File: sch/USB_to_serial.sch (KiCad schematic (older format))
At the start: 4 parts, among them J2 USB_B_Micro, U2 CP2102, U4 TPD2S017

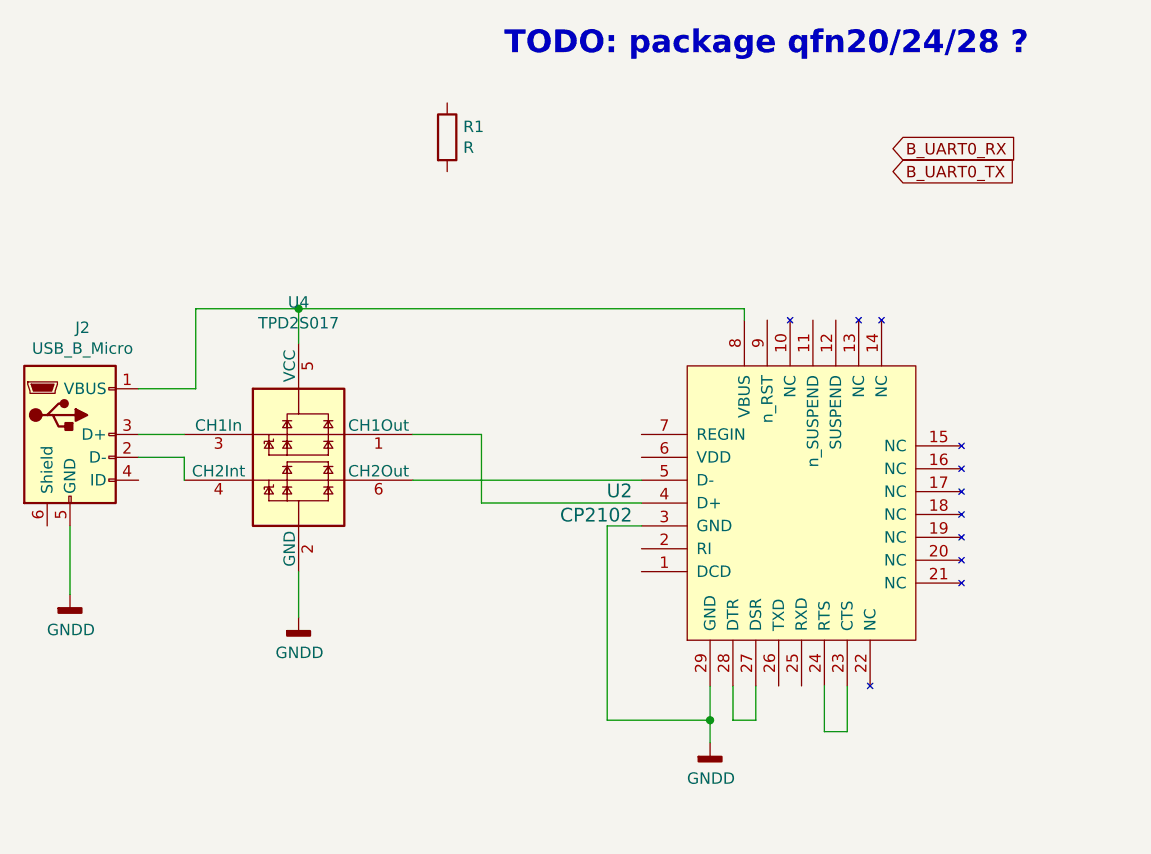
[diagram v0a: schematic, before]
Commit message: add u-boot sources
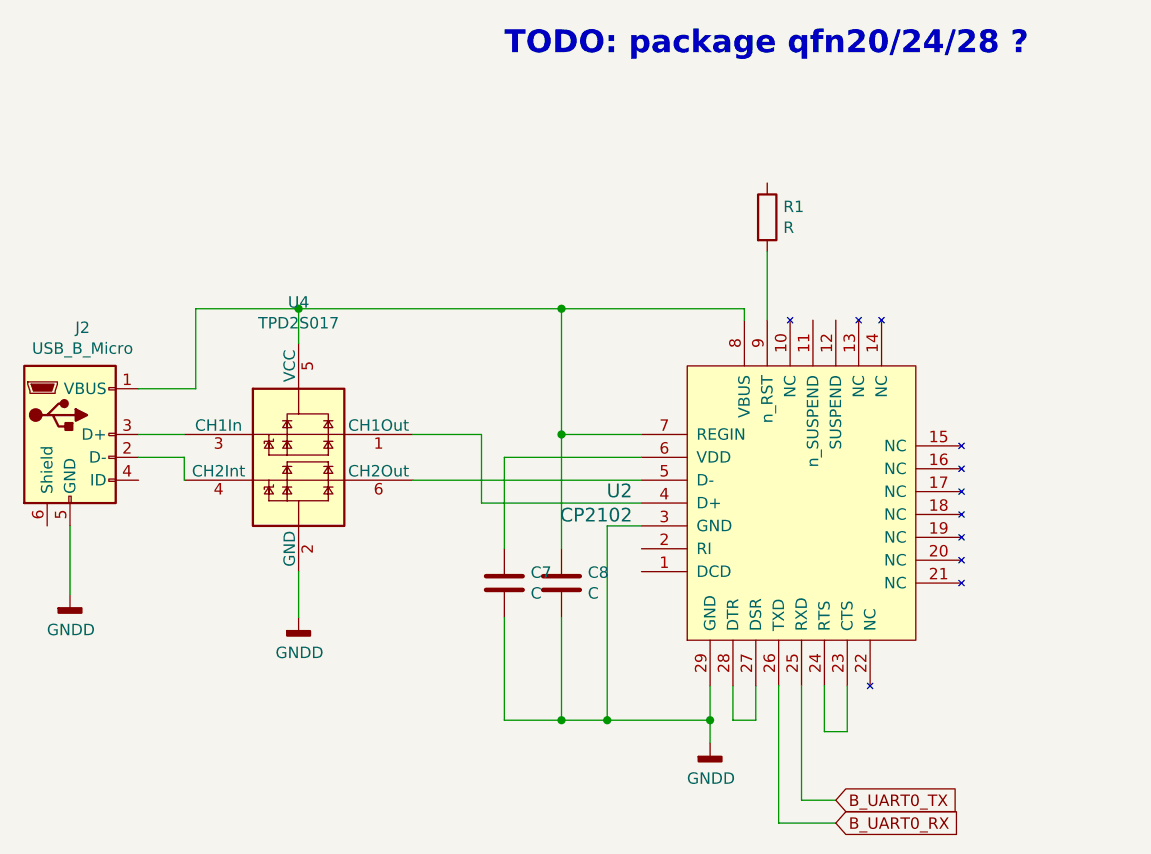
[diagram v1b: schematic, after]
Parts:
- added C7, C8: C, Capacitor_SMD:C_0805_2012Metric, symbol Device:C
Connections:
- net B_UART0_RX: now also U2.26 (TXD)
- net B_UART0_TX: now also U2.25 (RXD)
- net GNDD: now also C7.2, C8.1
- net at J2.1 (VBUS), U2.8 (VBUS), U4.5 (VCC): now also U2.7 (REGIN), C8.2
- net at R1.2: now also U2.9 (n_RST)
- net at U2.6 (VDD): now also C7.1
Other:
- moved on the sheet: R1
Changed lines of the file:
@@
 EESchema Schematic File Version 4
-LIBS:test-cache
-EELAYER 26 0
+EELAYER 30 0
 EELAYER END
 $Descr A4 11693 8268
@@
 Comment4 ""
 $EndDescr
-Text GLabel 6600 2750 2    50   Input ~ 0
+Text GLabel 6350 5700 2    50   Input ~ 0
 B_UART0_RX
-Text GLabel 6600 2850 2    50   Input ~ 0
+Text GLabel 6350 5600 2    50   Input ~ 0
 B_UART0_TX
 $Comp
@@
 L Device:R R1
 U 1 1 5ED061D5
-P 4650 2700
-F 0 "R1" H 4720 2746 50  0000 L CNN
-F 1 "R" H 4720 2655 50  0000 L CNN
-F 2 "Resistor_SMD:R_0603_1608Metric_Pad1.05x0.95mm_HandSolder" V 4580 2700 50  0001 C CNN
-F 3 "~" H 4650 2700 50  0001 C CNN
-	1    4650 2700
+P 6050 3050
+F 0 "R1" H 6120 3096 50  0000 L CNN
+F 1 "R" H 6120 3005 50  0000 L CNN
+F 2 "Resistor_SMD:R_0603_1608Metric_Pad1.05x0.95mm_HandSolder" V 5980 3050 50  0001 C CNN
+F 3 "~" H 6050 3050 50  0001 C CNN
+	1    6050 3050
 	1    0    0    -1
 $EndComp
@@
 	4500 4200 5500 4200
 Wire Wire Line
-	4000 3450 5950 3450
+	4000 3450 5150 3450
 Wire Wire Line
 	5950 3450 5950 3500
@@
 Wire Wire Line
 	6000 5250 6000 5100
+Wire Wire Line
+	5500 4000 5150 4000
+Wire Wire Line
+	5150 4000 5150 3450
+Connection ~ 5150 3450
+Wire Wire Line
+	5150 3450 5950 3450
+Wire Wire Line
+	6050 3500 6050 3200
+Wire Wire Line
+	6200 5100 6200 5600
+Wire Wire Line
+	6200 5600 6350 5600
+Wire Wire Line
+	6350 5700 6100 5700
+Wire Wire Line
+	6100 5700 6100 5100
+$Comp
+L Device:C C8
+U 1 1 5F2B1BE6
+P 5150 4650
+F 0 "C8" H 5035 4604 50  0000 R CNN
+F 1 "C" H 5035 4695 50  0000 R CNN
+F 2 "Capacitor_SMD:C_0805_2012Metric" H 5188 4500 50  0001 C CNN
+F 3 "~" H 5150 4650 50  0001 C CNN
+	1    5150 4650
+	-1   0    0    1
+$EndComp
+$Comp
+L Device:C C7
+U 1 1 5F2B6F97
+P 4900 4650
+F 0 "C7" H 5015 4696 50  0000 L CNN
+F 1 "C" H 5015 4605 50  0000 L CNN
+F 2 "Capacitor_SMD:C_0805_2012Metric" H 4938 4500 50  0001 C CNN
+F 3 "~" H 4900 4650 50  0001 C CNN
+	1    4900 4650
+	1    0    0    -1
+$EndComp
+Wire Wire Line
+	4900 4100 4900 4500
+Wire Wire Line
+	4900 4100 5500 4100
+Wire Wire Line
+	5150 4000 5150 4500
+Connection ~ 5150 4000
+Wire Wire Line
+	5350 5250 5150 5250
+Wire Wire Line
+	4900 5250 4900 4800
+Connection ~ 5350 5250
+Wire Wire Line
+	5150 4800 5150 5250
+Connection ~ 5150 5250
+Wire Wire Line
+	5150 5250 4900 5250
 $EndSCHEMATC
